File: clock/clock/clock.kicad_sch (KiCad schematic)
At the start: 50 parts, among them J1 AVR-ISP-6, J10 Conn_01x07_Male, J11 CV_IN, J12 BEAT_OUT, J13 DIV_OUT, J14 SCREW1, J15 BEAT_OUT, J16 DIV_OUT, J17 CV_IN, J18 KNOB, J19 SCREW2, J2 EURORACK_CONN_10, J3 Conn_01x05_Female, J4 Conn_01x05_Male, J5 Conn_01x05_Female, J6 Conn_01x05_Male, J7 Conn_01x05_Female, J8 Conn_01x05_Male, J9 Conn_01x07_Female, SW1 SW_Push, SW2 SW_Push, SW3 Rotary_Encoder_Switch, U1 ATmega328P-PU, U2 L7805, U3 SM460281N, U4 SM460281N, U5 SM460281N, Y1 16MHz

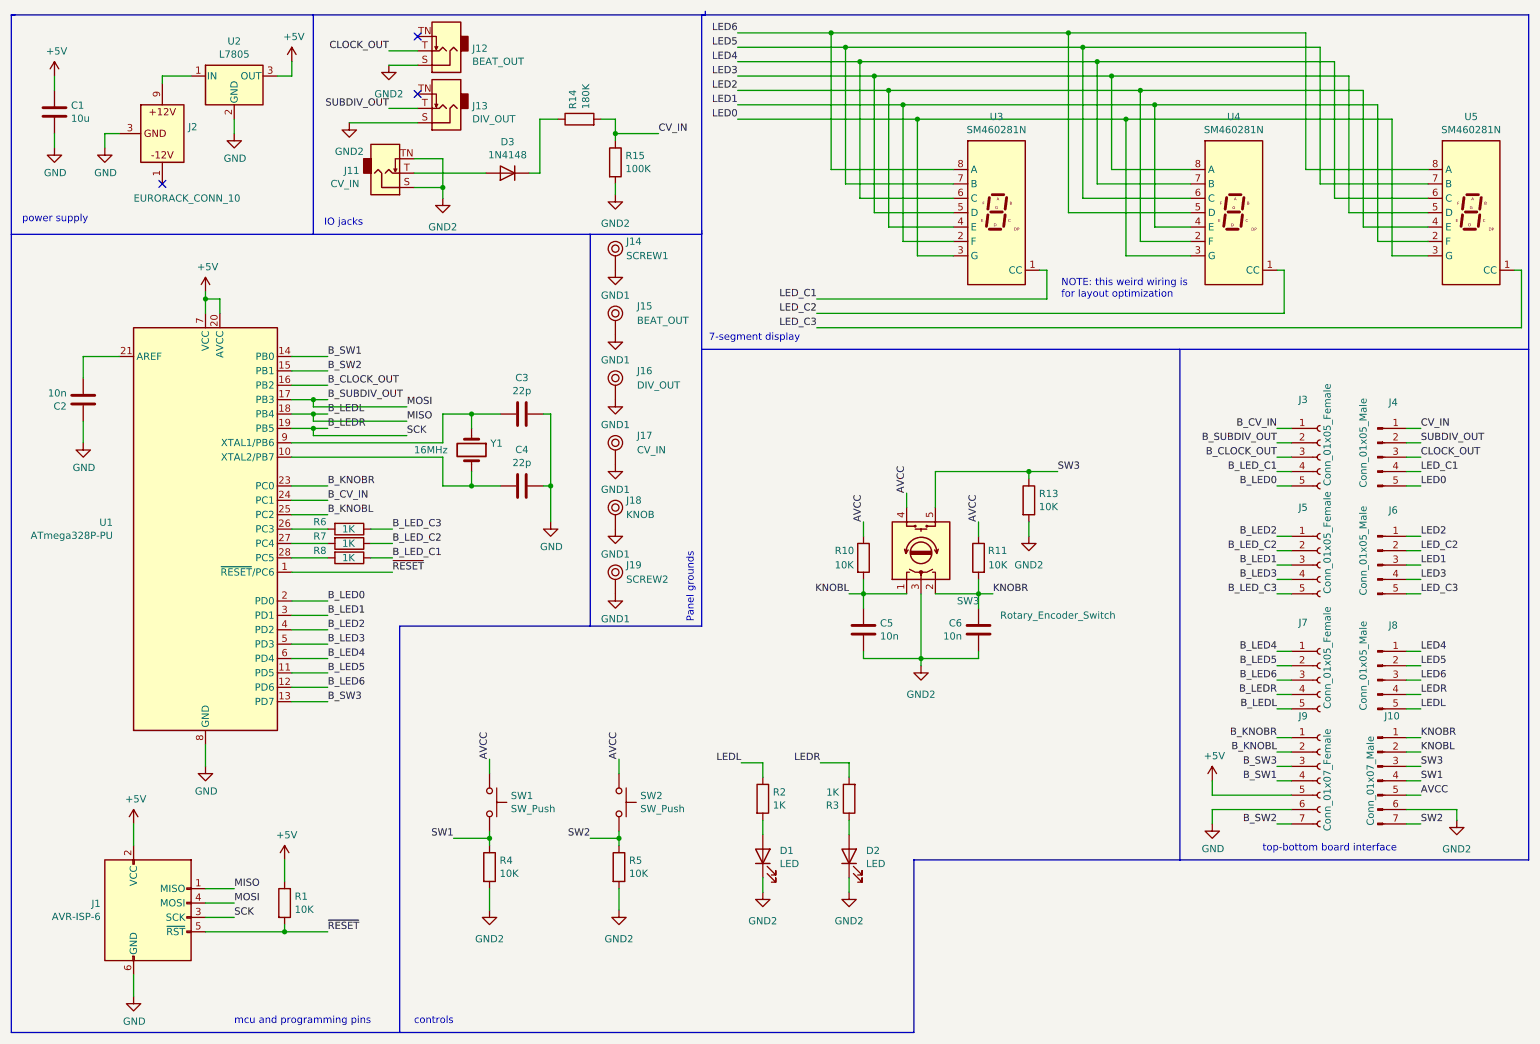
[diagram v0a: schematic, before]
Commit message: convert clock project to KiCad 10 file format
Upgraded via kicad-cli sch/pcb upgrade. Needed for outline (TTF)
font support on silkscreen text, which arrived in KiCad 7.
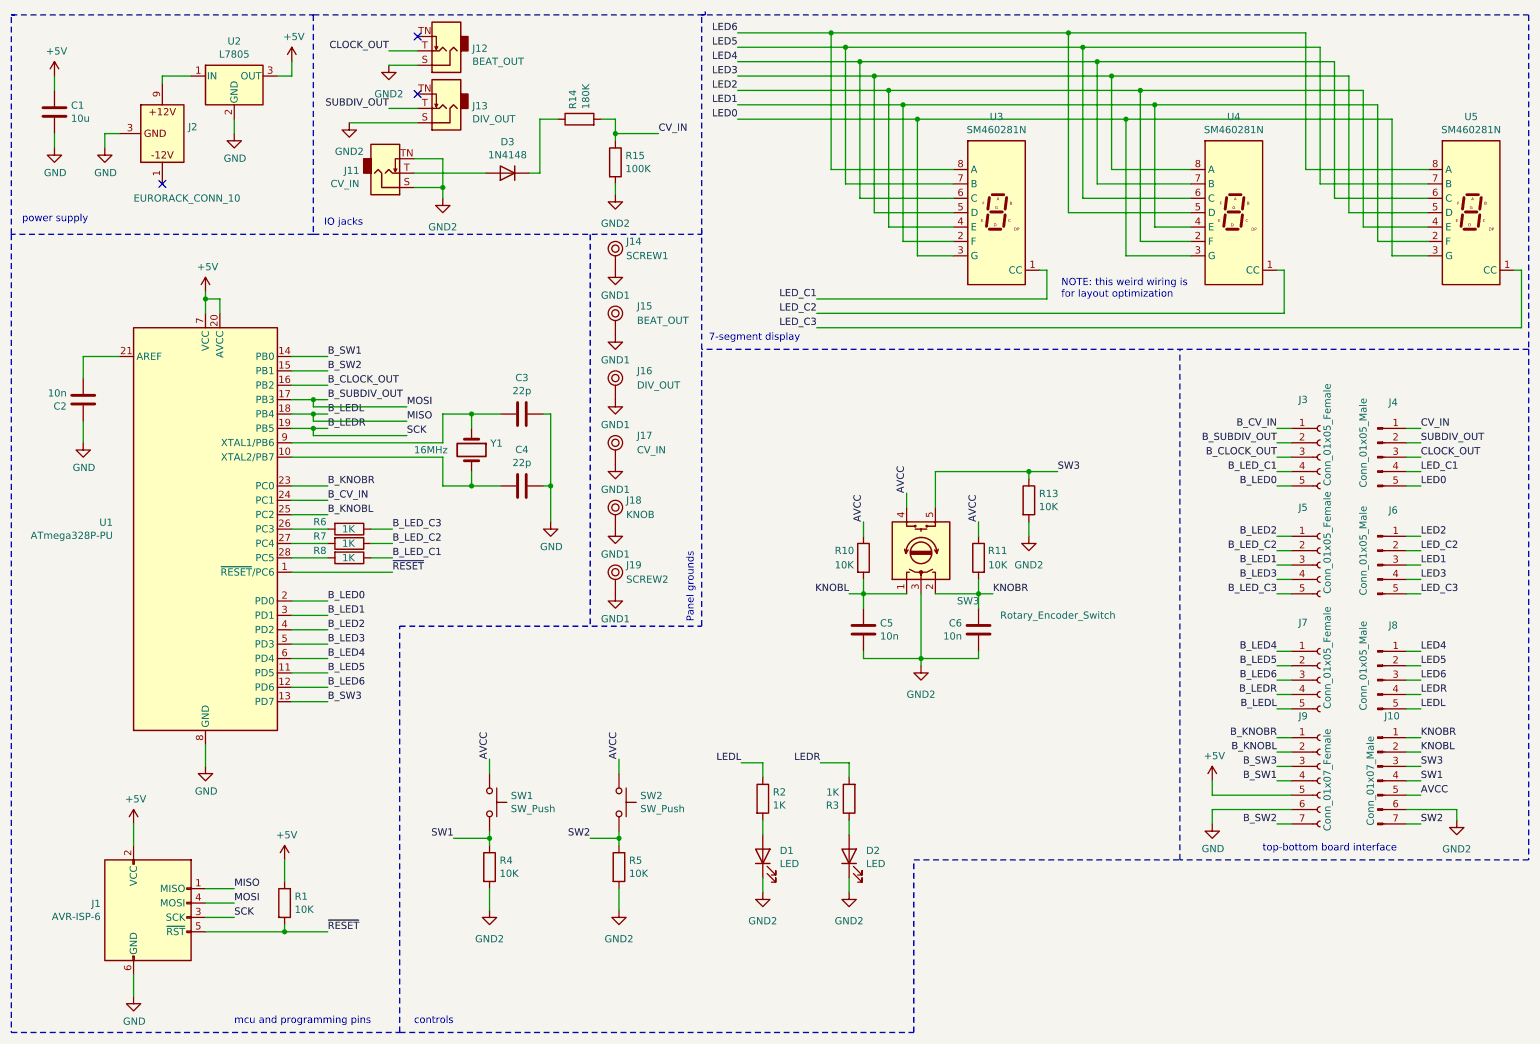
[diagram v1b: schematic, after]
